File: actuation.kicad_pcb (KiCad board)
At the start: 4 copper layers, 320 parts, among them J1 ACTUATION, J10 ACT CH9, J11 ACT CH10, J12 ACT CH11, J13 ACT CH12, J14 ACT CH13, J15 ACT CH14, J16 ACT CH15, J17 ACT CH16, J18 FB CH1, J19 FB CH2, J2 ACT CH1, J20 FB CH3, J21 VDET CH1, J22 VDET CH2, J23 PWR IN, J24 PWR PROT, J25 PWR 3.3V, J26 SAFETY, J27 ARM, J28 ACT HOT, J29 ACT COLD, J3 ACT CH2, J4 ACT CH3, J5 ACT CH4, J6 ACT CH5, J7 ACT CH6, J8 ACT CH7, J9 ACT CH8, K1 J115F11C, Q1 SI7220 NMOS, Q2 NMOS, U1 TPD4E02B04DQA, U10 TLP241A, U11 TLP241A, U12 TLP241A, U13 TLP241A, U14 TLP241A, U15 TLP241A, U16 TLP241A, U17 TLP241A, U18 TLP241A, U19 PCA9534, U2 PCA9615, U20 PCA9534, U21 TLP2366, U22 TLP2366, U23 TLP2366, U24 TLP2366, U25 TLP2366, U26 TLP2366, U27 TLV7031, U28 TLV7031, U29 TLP2366, U3 TLP241A, U30 TLP2366, U31 74LVC1G126, U32 74LVC1G126, U33 PCA9534, U34 SN74LVC541A, U35 TLI4971, U36 LTC4367, U37 ADS1110, U38 AP64350, U39 TLP241A, U4 TLP241A, U40 LP5912-3.3DRV, U5 TLP241A, U6 TLP241A, U7 TLP241A, U8 TLP241A, U9 TLP241A

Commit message: much denser, should be no stray footprints now
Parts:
- moved R44 259.1 mm to (259.0, 144.8), turned to 180 degrees
- moved U21 251.3 mm to (252.6, 143.9), turned to 180 degrees
- moved C25 250.8 mm to (246.8, 145.3), turned to 180 degrees
- moved R58 241.4 mm to (259.5, 152.0), turned to -90 degrees
- moved R59 239.7 mm to (259.5, 148.8), turned to -90 degrees
- moved U32 239.0 mm to (256.0, 150.3), turned to 180 degrees
- moved R55 229.6 mm to (253.0, 150.3), turned to -90 degrees
- moved U30 218.5 mm to (247.5, 150.3), turned to 180 degrees
- moved C32 218.3 mm to (247.3, 153.8)
- moved TP8 217.8 mm to (244.8, 133.8), turned to 90 degrees
- moved R54 209.5 mm to (252.5, 154.5)
- moved R56 206.1 mm to (260.0, 157.3), turned to -90 degrees
- moved R75 206.1 mm to (242.8, 126.3), turned to 90 degrees
- moved R74 204.8 mm to (241.3, 126.3), turned to 90 degrees
- moved R57 204.1 mm to (258.5, 157.3), turned to 90 degrees
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
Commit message: moved whole thing to center of page
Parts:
- moved J29 168.9 mm to (83.8, 49.9)
- moved J24 168.9 mm to (83.6, 59.6)
- moved J25 168.9 mm to (83.9, 69.7)
- moved J28 168.9 mm to (83.7, 40.2)
- moved C40 72.7 mm to (163.6, 105.1)
- moved C37 72.7 mm to (169.5, 110.7)
- moved U36 72.7 mm to (168.6, 105.5)
- moved C38 72.7 mm to (167.2, 85.7)
- moved C39 72.7 mm to (165.4, 105.1)
- moved C49 72.7 mm to (175.7, 98.9)
- moved C52 72.7 mm to (176.7, 103.7)
- moved C53 72.7 mm to (179.7, 103.7)
- moved C56 72.7 mm to (177.2, 74.2)
- moved C59 72.7 mm to (174.7, 77.7)
- moved C60 72.7 mm to (177.2, 81.7)
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
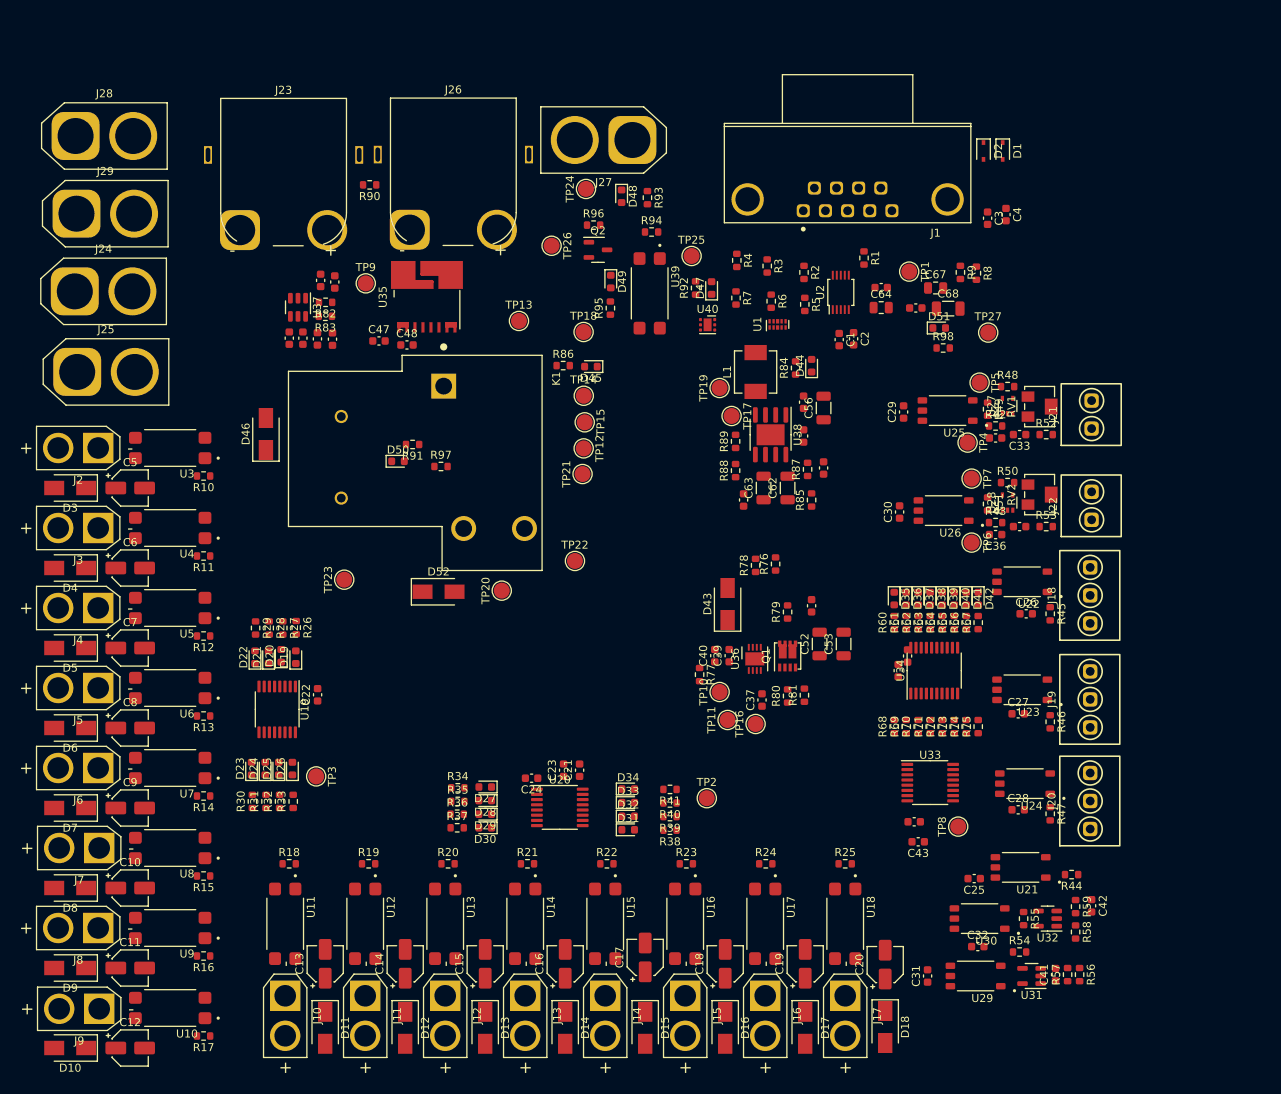
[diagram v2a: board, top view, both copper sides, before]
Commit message: arranged power supplies
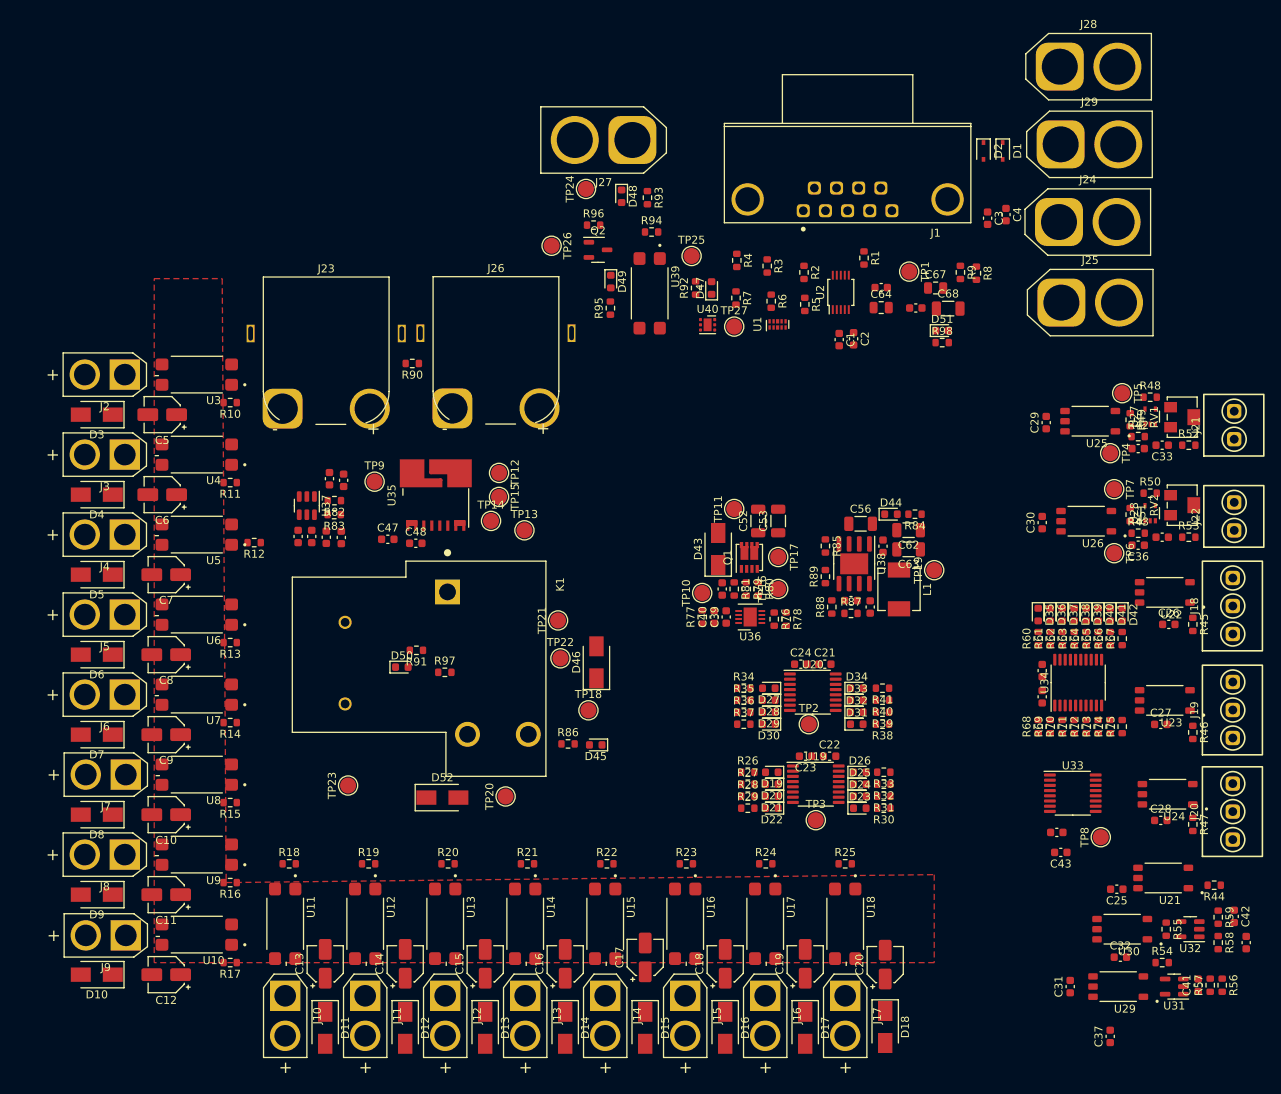
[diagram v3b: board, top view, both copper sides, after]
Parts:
- moved J25 123.3 mm to (206.9, 61.0)
- moved J29 123.3 mm to (206.8, 41.2)
- moved J24 123.3 mm to (206.6, 50.9)
- moved J28 123.3 mm to (206.7, 31.5)
- moved C38 83.7 mm to (230.0, 141.0)
- moved R30 78.9 mm to (184.7, 124.2), turned to 180 degrees
- moved R31 77.2 mm to (184.7, 122.7), turned to 180 degrees
- moved D23 76.2 mm to (181.7, 124.2), turned to 0 degrees
- moved R32 75.6 mm to (184.7, 121.2), turned to 180 degrees
- moved D24 74.4 mm to (181.7, 122.7), turned to 0 degrees
- moved R33 73.9 mm to (184.7, 119.7), turned to 180 degrees
- moved D25 72.7 mm to (181.7, 121.2), turned to 0 degrees
- moved D26 70.9 mm to (181.7, 119.7), turned to 0 degrees
- moved U19 68.0 mm to (176.2, 121.2), turned to 0 degrees
- moved D22 67.3 mm to (170.7, 124.2), turned to 180 degrees
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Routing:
- added copper zone on F.Cu, net Vdrive

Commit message: roughly determine board outline
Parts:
- added REF**: MountingHole_3.2mm_M3, MountingHole:MountingHole_3.2mm_M3, F.Cu at (84.0, 136.0)
- J10, J11, J12, J13, J14, J15, J16, J17, J2, J3, J4, J5, J6, J7, J8, J9: footprint Connector_AMASS:AMASS_XT30U-M_1x02_P5.0mm_Vertical -> actuation:XT30U-M
- J18, J19, J20: footprint actuation:1751251 -> actuation:1935174
- J21, J22: footprint actuation:1751248 -> actuation:1935161
- moved J29 147.9 mm to (92.5, 135.0), turned to 90 degrees
- moved J28 147.2 mm to (102.0, 135.0), turned to 90 degrees
- moved J24 84.2 mm to (202.0, 135.0), turned to 90 degrees
- moved J25 75.4 mm to (192.5, 135.0), turned to 90 degrees
- moved C22 39.0 mm to (174.0, 78.9)
- moved C23 39.0 mm to (171.0, 78.9)
- moved R38 39.0 mm to (180.6, 74.9)
- moved R39 39.0 mm to (180.6, 73.4)
- moved R40 39.0 mm to (180.6, 71.9)
- moved R41 39.0 mm to (180.6, 70.4)
- moved C21 39.0 mm to (173.4, 67.4)
- moved C24 39.0 mm to (170.4, 67.4)
- moved D19 39.0 mm to (166.8, 80.9)
- moved D20 39.0 mm to (166.8, 82.4)
- moved D21 39.0 mm to (166.8, 83.9)
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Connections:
- net Net-(D46-Pad1) renamed /Power/COIL+
- net Net-(D46-Pad2) renamed /Power/COIL-
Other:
- board outline added: 150 x 100 mm

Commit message: 100x130
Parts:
- added REF**: MountingHole_3.2mm_M3, MountingHole:MountingHole_3.2mm_M3, F.Cu at (85.0, 45.0)
- added REF**: MountingHole_3.2mm_M3, MountingHole:MountingHole_3.2mm_M3, F.Cu at (205.0, 135.0)
- added REF**: MountingHole_3.2mm_M3, MountingHole:MountingHole_3.2mm_M3, F.Cu at (205.0, 45.0)
- moved J29 90.1 mm to (95.9, 45.0), turned to 0 degrees
- moved C57 63.7 mm to (170.9, 64.6), turned to 90 degrees
- moved C58 60.4 mm to (169.2, 64.6), turned to 90 degrees
- moved U37 60.1 mm to (169.8, 68.5), turned to 90 degrees
- moved C55 56.9 mm to (167.4, 64.5), turned to 90 degrees
- moved TP23 54.8 mm to (151.5, 69.5)
- moved C54 54.1 mm to (167.0, 71.8), turned to -90 degrees
- moved R83 53.7 mm to (166.4, 67.4), turned to 0 degrees
- moved C51 53.3 mm to (165.5, 64.5), turned to 90 degrees
- moved R82 53.2 mm to (166.4, 69.1), turned to 0 degrees
- moved C50 50.5 mm to (165.2, 71.6), turned to -90 degrees
- moved C43 42.3 mm to (174.3, 84.0)
- moved C45 41.8 mm to (174.0, 82.0)
- moved TP8 41.3 mm to (172.8, 92.5)
- moved C32 41.1 mm to (179.0, 102.0), turned to 90 degrees
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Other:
- board size 150 x 100 mm -> 130 x 100 mm
- board text added: "100 x 130 mm"

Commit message: Revert "100x130"
This reverts commit c49d85ffcdfed8898d048473301597551dfc5cab.
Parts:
- removed the REF** at (85.0, 45.0)
- removed the REF** at (205.0, 135.0)
- removed the REF** at (205.0, 45.0)
- moved J29 90.1 mm to (92.5, 135.0), turned to 90 degrees
- moved C57 63.7 mm to (109.0, 79.4), turned to -90 degrees
- moved C58 60.4 mm to (110.7, 79.4), turned to -90 degrees
- moved U37 60.1 mm to (110.1, 75.6), turned to -90 degrees
- moved C55 56.9 mm to (112.5, 79.5), turned to -90 degrees
- moved TP23 54.8 mm to (115.2, 110.6)
- moved C54 54.1 mm to (112.9, 72.2), turned to 90 degrees
- moved R83 53.7 mm to (113.5, 76.7), turned to 180 degrees
- moved C51 53.3 mm to (114.4, 79.6), turned to -90 degrees
- moved R82 53.2 mm to (113.5, 75.0), turned to 180 degrees
- moved C50 50.5 mm to (114.7, 72.4), turned to 90 degrees
- moved C43 42.3 mm to (204.3, 113.7)
- moved C45 41.8 mm to (203.8, 111.2)
- moved TP8 41.3 mm to (209.3, 111.8)
- moved C32 41.1 mm to (211.8, 126.8), turned to 0 degrees
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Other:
- board size 130 x 100 mm -> 150 x 100 mm
- board text removed: "100 x 130 mm"
